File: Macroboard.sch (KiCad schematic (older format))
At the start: 34 parts, among them SW1 SW_Push, U1 ATmega32U4-AU, Y1 16MHz

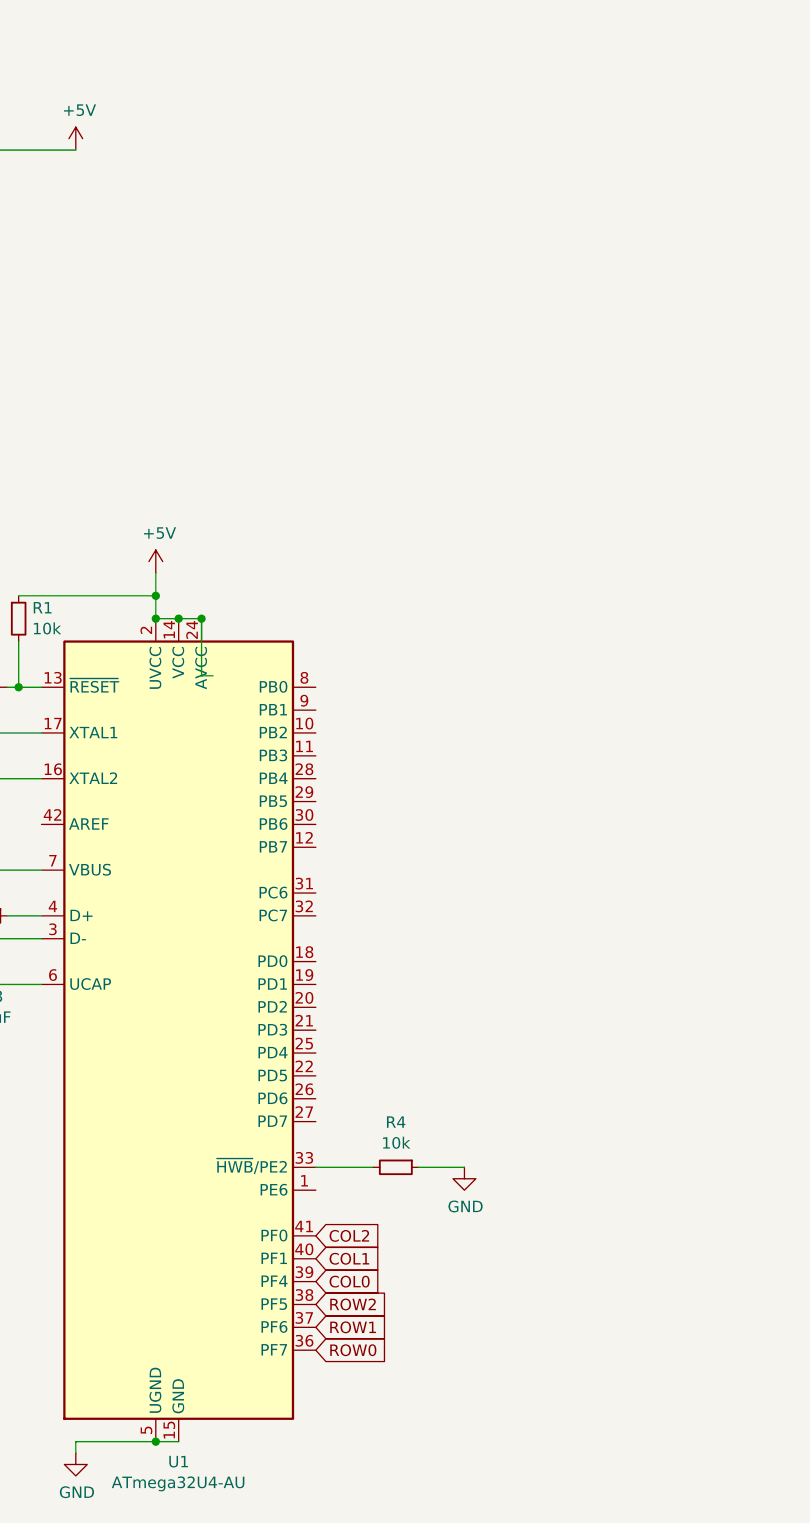
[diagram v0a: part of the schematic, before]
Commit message: mounting holes to PCB
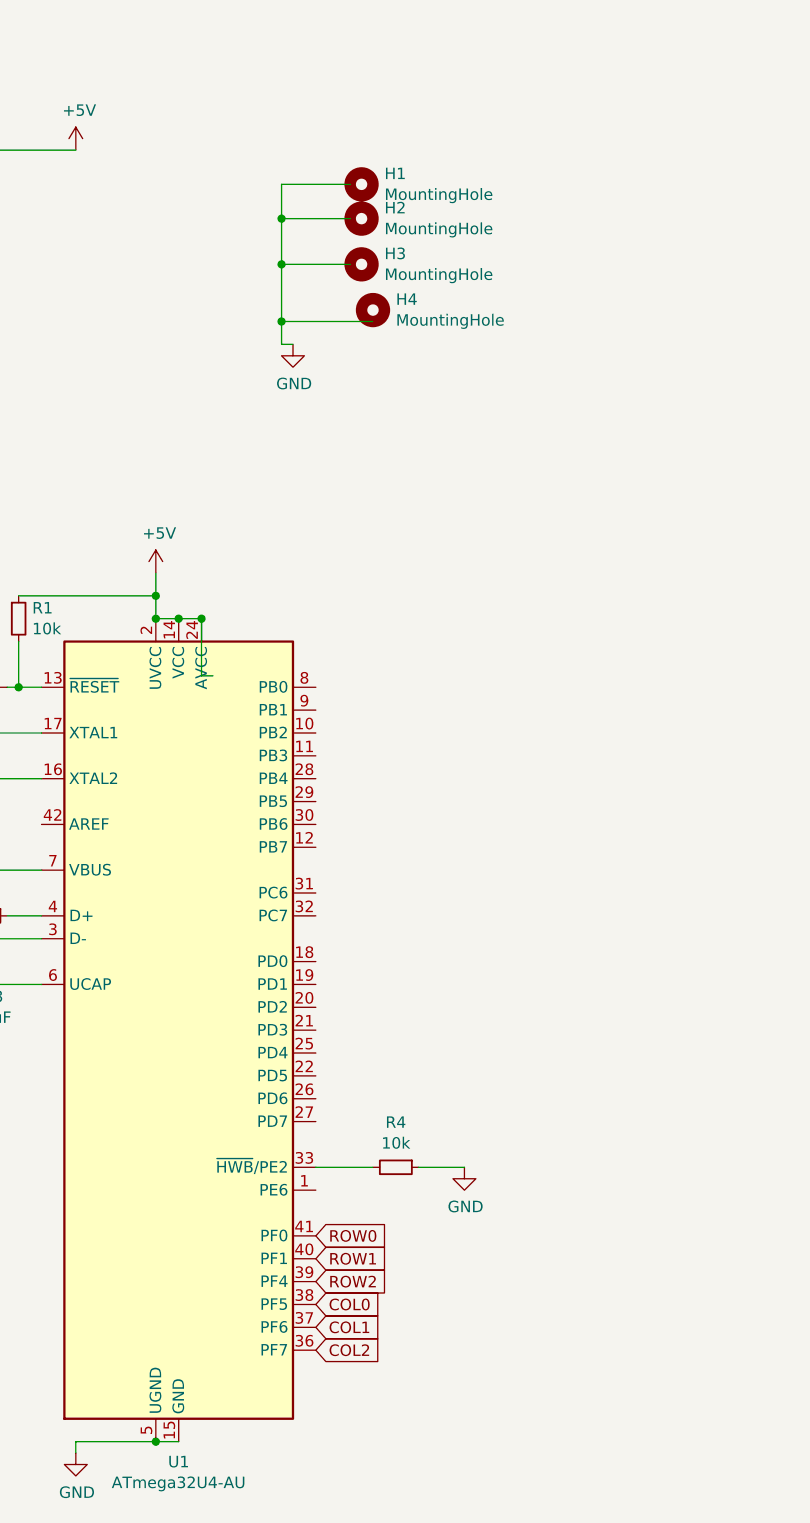
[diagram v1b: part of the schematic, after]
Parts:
- added H1, H2, H3, H4: MountingHole, MountingHole:MountingHole_2.2mm_M2_Pad_Via, symbol Mechanical:MountingHole
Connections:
- wire segments 77 -> 86
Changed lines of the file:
@@
 Text GLabel 7750 3650 0    50   Input ~ 0
 ROW2
+Text GLabel 4200 5800 2    50   Input ~ 0
+ROW0
+Text GLabel 4200 5900 2    50   Input ~ 0
+ROW1
+Text GLabel 4200 6000 2    50   Input ~ 0
+ROW2
+Text GLabel 4200 6100 2    50   Input ~ 0
+COL0
+Text GLabel 4200 6200 2    50   Input ~ 0
+COL1
 Text GLabel 4200 6300 2    50   Input ~ 0
-ROW0
-Text GLabel 4200 6200 2    50   Input ~ 0
-ROW1
-Text GLabel 4200 6100 2    50   Input ~ 0
-ROW2
-Text GLabel 4200 6000 2    50   Input ~ 0
-COL0
-Text GLabel 4200 5900 2    50   Input ~ 0
-COL1
-Text GLabel 4200 5800 2    50   Input ~ 0
 COL2
+$Comp
+L Mechanical:MountingHole H4
+U 1 1 5DB4BB8B
+P 4450 1750
+F 0 "H4" H 4550 1796 50  0000 L CNN
+F 1 "MountingHole" H 4550 1705 50  0000 L CNN
+F 2 "MountingHole:MountingHole_2.2mm_M2_Pad_Via" H 4450 1750 50  0001 C CNN
+F 3 "~" H 4450 1750 50  0001 C CNN
+	1    4450 1750
+	1    0    0    -1
+$EndComp
+$Comp
+L Mechanical:MountingHole H3
+U 1 1 5DB4CB38
+P 4400 1550
+F 0 "H3" H 4500 1596 50  0000 L CNN
+F 1 "MountingHole" H 4500 1505 50  0000 L CNN
+F 2 "MountingHole:MountingHole_2.2mm_M2_Pad_Via" H 4400 1550 50  0001 C CNN
+F 3 "~" H 4400 1550 50  0001 C CNN
+	1    4400 1550
+	1    0    0    -1
+$EndComp
+$Comp
+L Mechanical:MountingHole H2
+U 1 1 5DB4D436
+P 4400 1350
+F 0 "H2" H 4500 1396 50  0000 L CNN
+F 1 "MountingHole" H 4500 1305 50  0000 L CNN
+F 2 "MountingHole:MountingHole_2.2mm_M2_Pad_Via" H 4400 1350 50  0001 C CNN
+F 3 "~" H 4400 1350 50  0001 C CNN
+	1    4400 1350
+	1    0    0    -1
+$EndComp
+$Comp
+L Mechanical:MountingHole H1
+U 1 1 5DB4D5FE
+P 4400 1200
+F 0 "H1" H 4500 1246 50  0000 L CNN
+F 1 "MountingHole" H 4500 1155 50  0000 L CNN
+F 2 "MountingHole:MountingHole_2.2mm_M2_Pad_Via" H 4400 1200 50  0001 C CNN
+F 3 "~" H 4400 1200 50  0001 C CNN
+	1    4400 1200
+	1    0    0    -1
+$EndComp
+$Comp
+L power:GND #PWR0113
+U 1 1 5DB50CE9
+P 4100 1900
+F 0 "#PWR0113" H 4100 1650 50  0001 C CNN
+F 1 "GND" H 4105 1727 50  0000 C CNN
+F 2 "" H 4100 1900 50  0001 C CNN
+F 3 "" H 4100 1900 50  0001 C CNN
+	1    4100 1900
+	1    0    0    -1
+$EndComp
+Wire Wire Line
+	4350 1200 4050 1200
+Wire Wire Line
+	4050 1200 4050 1350
+Wire Wire Line
+	4050 1900 4100 1900
+Wire Wire Line
+	4350 1350 4050 1350
+Connection ~ 4050 1350
+Wire Wire Line
+	4050 1350 4050 1550
+Wire Wire Line
+	4350 1550 4050 1550
+Connection ~ 4050 1550
+Wire Wire Line
+	4050 1550 4050 1800
+Wire Wire Line
+	4450 1800 4050 1800
+Connection ~ 4050 1800
+Wire Wire Line
+	4050 1800 4050 1900
 $EndSCHEMATC

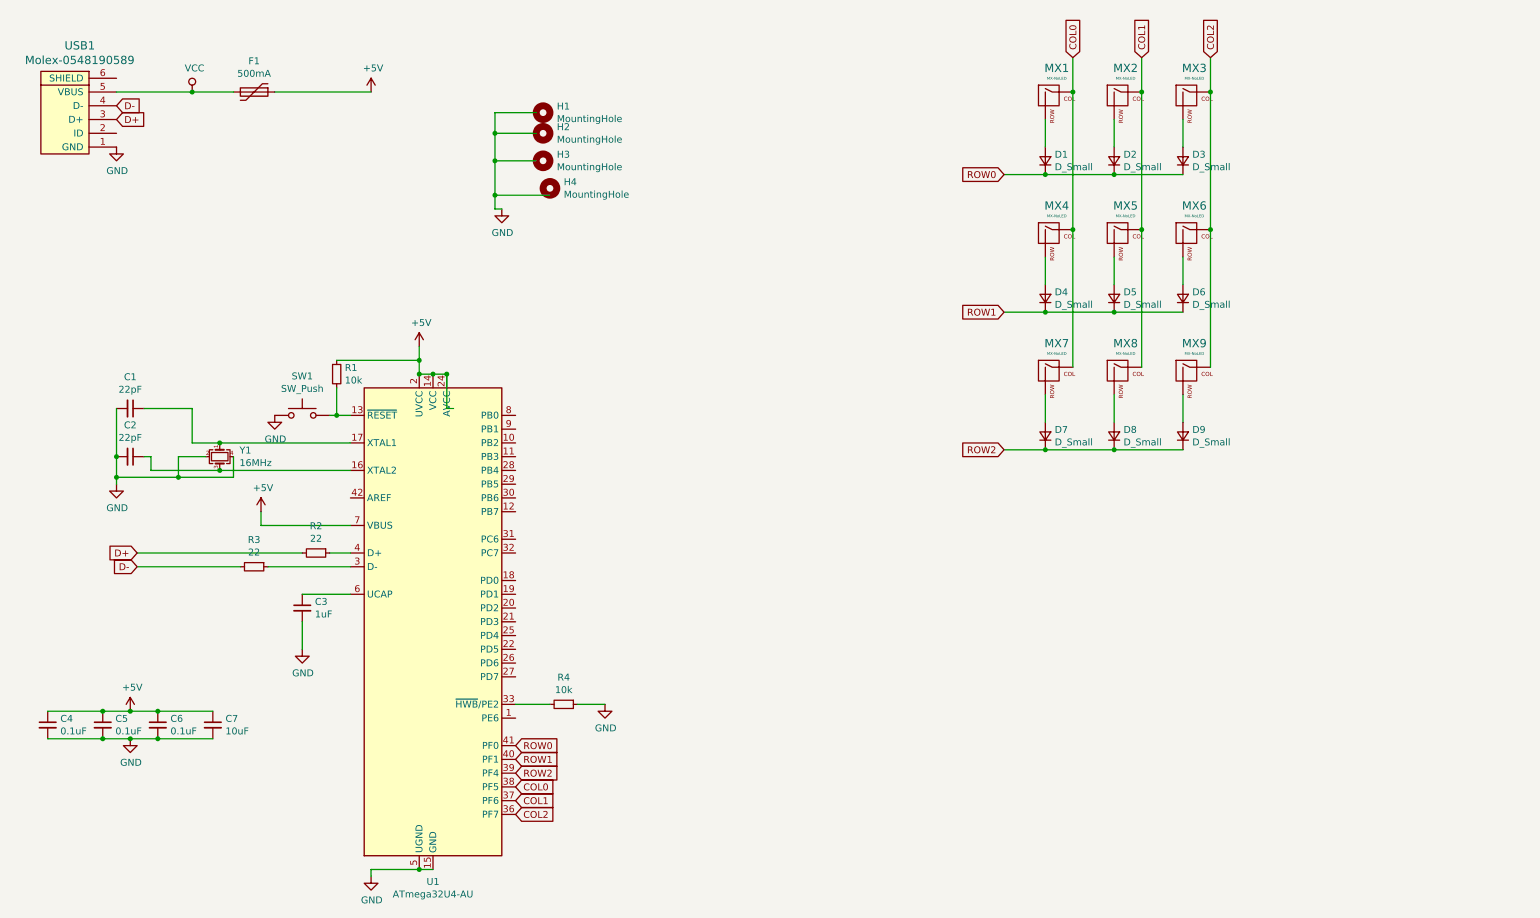
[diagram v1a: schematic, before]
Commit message: LED-switches added
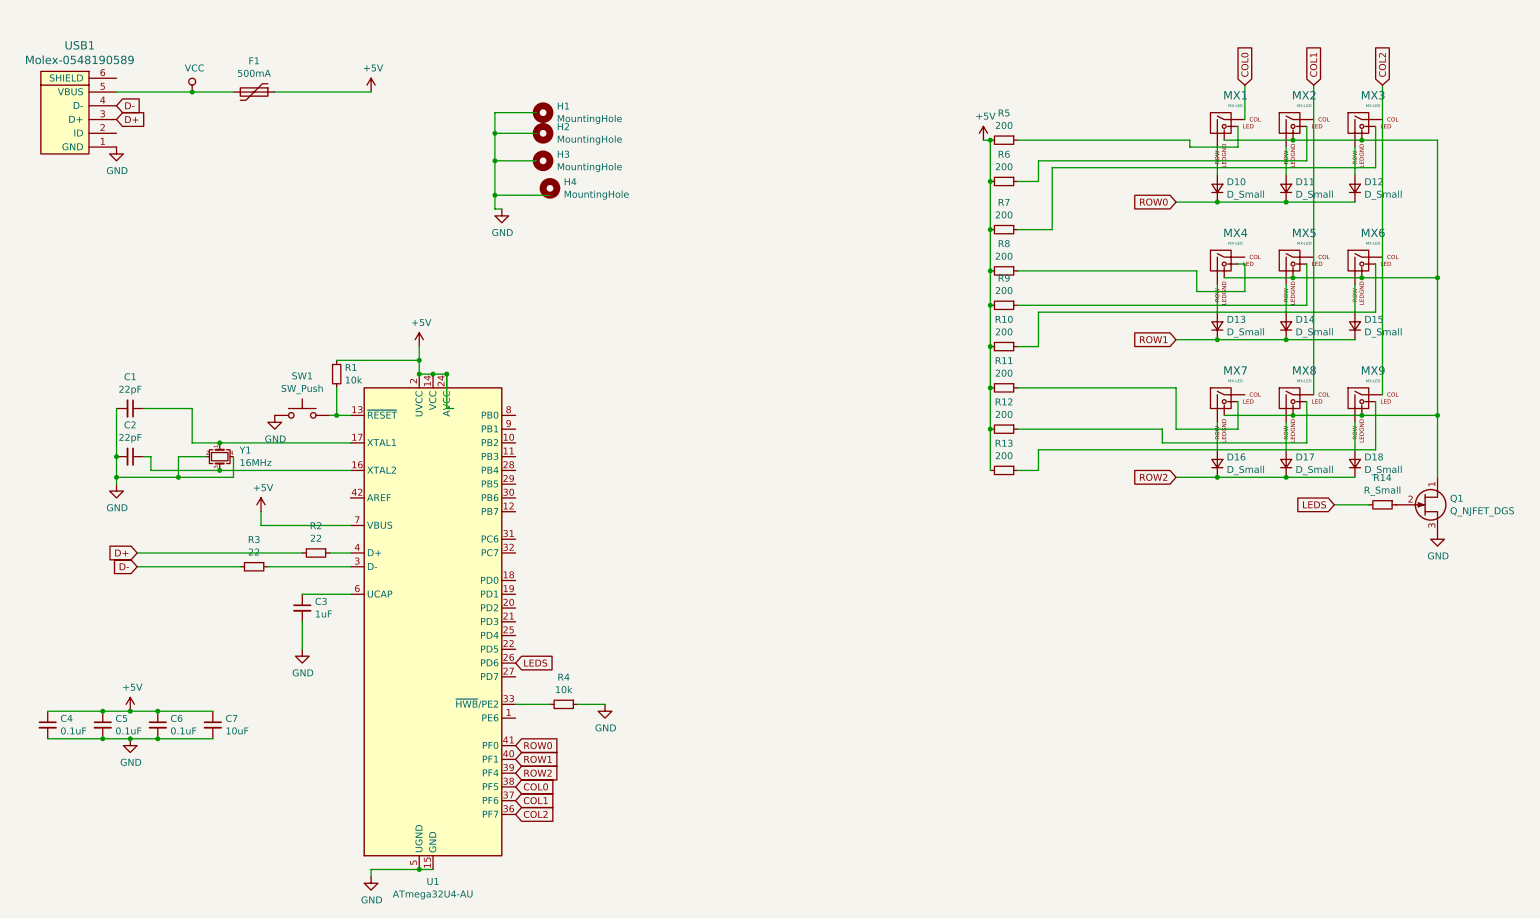
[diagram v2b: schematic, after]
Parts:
- removed D1, D2, D3, D4, D5, D6, D7, D8, D9: D_Small, Diode_SMD:D_SOD-123, symbol Device:D_Small
- removed MX1, MX2, MX3, MX4, MX5, MX6, MX7, MX8, MX9: MX-NoLED, MX_Only:MXOnly-1U-NoLED, symbol MX_Alps_Hybrid:MX-NoLED
- added D10, D11, D12, D13, D14, D15, D16, D17, D18: D_Small, Diode_SMD:D_SOD-123, symbol Device:D_Small
- added MX1, MX2, MX3, MX4, MX5, MX6, MX7, MX8, MX9: MX-LED, MX_Only:MXOnly-1U, symbol MX_Alps_Hybrid:MX-LED
- added Q1: Q_NJFET_DGS, symbol Device:Q_NJFET_DGS
- added R10, R11, R12, R13, R5, R6, R7, R8, R9: 200, Resistor_SMD:R_0603_1608Metric_Pad1.05x0.95mm_HandSolder, symbol Device:R_Small
- added R14: R_Small, Resistor_SMD:R_0603_1608Metric_Pad1.05x0.95mm_HandSolder, symbol Device:R_Small
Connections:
- net labels added: LEDS
- wire segments 86 -> 137
